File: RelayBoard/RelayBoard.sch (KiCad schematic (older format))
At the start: 56 parts, among them J1 Micro_SD_Card, J10 Conn_01x04_Male, J11 Conn_01x04_Male, J13 Conn_01x04_Male, J2 Screw_Terminal_01x02, J3 Conn_01x04_Male, J4 Conn_01x04_Male, J5 Conn_01x04_Male, J7 SI-52008-F, J8 SI-52008-F, J9 Conn_01x04_Male, U1 STM32F745VEHx, U2 KSZ8863RLL, U3 TJA1051T-3, U4 LF33_TO252, X1 ECS-2520MV-xxx-xx

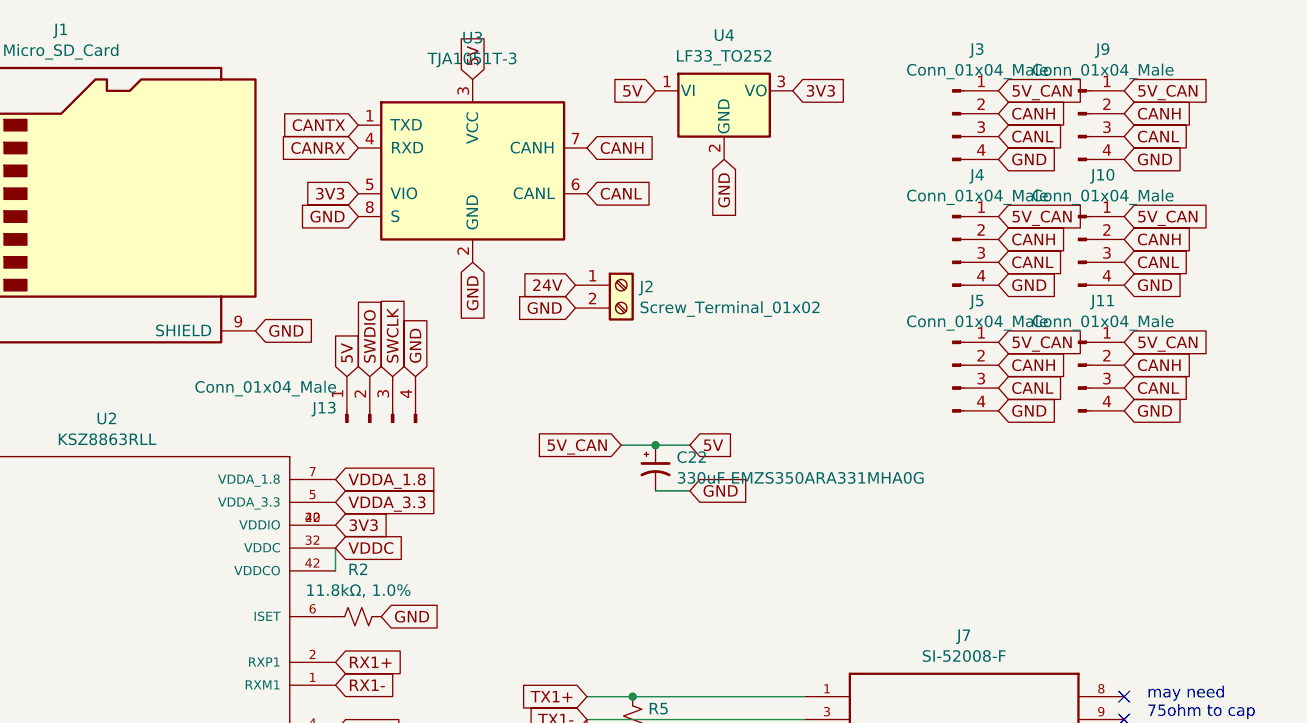
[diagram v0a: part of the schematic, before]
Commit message: unnecessary but satisfying miniaturization
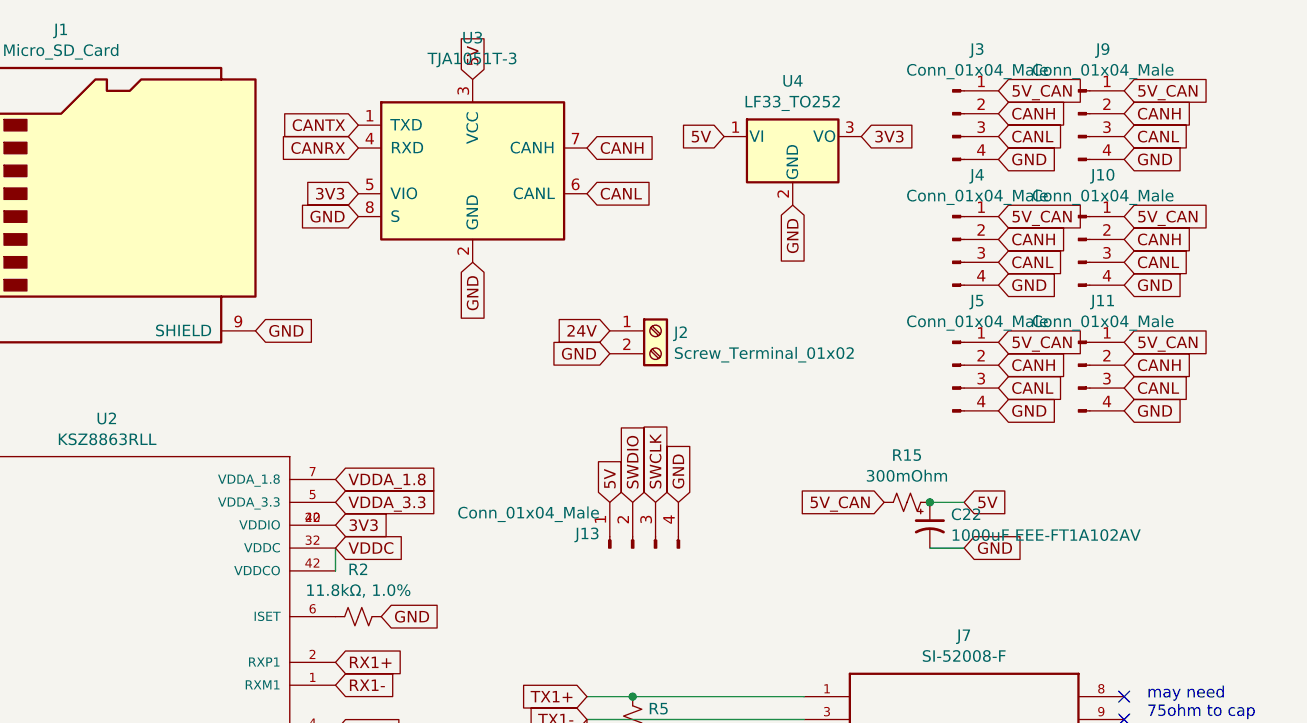
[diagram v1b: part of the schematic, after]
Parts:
- added R15: 300mOhm, symbol Device:R_Small_US
- C22: value 330uF EMZS350ARA331MHA0G -> 1000uF EEE-FT1A102AV; footprint Capacitor_SMD:CP_Elec_10x10 -> Capacitor_SMD:CP_Elec_8x10.5
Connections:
- net +5V: now also R15.1; no longer J10.1 (Pin_1), J11.1 (Pin_1), J3.1 (Pin_1), J4.1 (Pin_1), J5.1 (Pin_1), J9.1 (Pin_1)
- new net 5V_CAN: J10.1 (Pin_1), J11.1 (Pin_1), J3.1 (Pin_1), J4.1 (Pin_1), J5.1 (Pin_1), J9.1 (Pin_1), R15.2
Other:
- moved on the sheet: C22, J13, J2, U4
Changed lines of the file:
@@
 Comment4 ""
 $EndDescr
-$Comp
-L Connector:Screw_Terminal_01x02 J2
-U 1 1 5E6836EC
-P 7600 1650
-F 0 "J2" H 7680 1642 50  0000 L CNN
-F 1 "Screw_Terminal_01x02" H 7680 1551 50  0000 L CNN
-F 2 "TerminalBlock_Phoenix:TerminalBlock_Phoenix_MKDS-1,5-2_1x02_P5.00mm_Horizontal" H 7600 1650 50  0001 C CNN
-F 3 "~" H 7600 1650 50  0001 C CNN
-	1    7600 1650
-	1    0    0    -1
-$EndComp
 Text GLabel 7450 1050 2    50   Input ~ 0
 CANH
@@
 Text GLabel 6450 1050 0    50   Input ~ 0
 CANRX
-$Comp
-L Interface_CAN_LIN:TJA1051T-3 U3
-U 1 1 5E6B6C50
-P 6950 1150
-F 0 "U3" H 6950 1731 50  0000 C CNN
-F 1 "TJA1051T-3" H 6950 1640 50  0000 C CNN
-F 2 "Package_SO:SOIC-8_3.9x4.9mm_P1.27mm" H 6950 650 50  0001 C CIN
-F 3 "http://www.nxp.com/documents/data_sheet/TJA1051.pdf" H 6950 1150 50  0001 C CNN
-	1    6950 1150
-	1    0    0    -1
-$EndComp
 Text GLabel 6950 1550 3    50   Input ~ 0
 GND
@@
 Text GLabel 6450 1250 0    50   Input ~ 0
 3V3
-Text GLabel 7400 1650 0    50   Input ~ 0
-24V
-Text GLabel 7400 1750 0    50   Input ~ 0
-GND
 $Comp
 L SI-52008-F:SI-52008-F J7
@@
 L Regulator_Linear:LF33_TO252 U4
 U 1 1 5E6D356C
-P 8050 800
-F 0 "U4" H 8050 1042 50  0000 C CNN
-F 1 "LF33_TO252" H 8050 951 50  0000 C CNN
-F 2 "Package_TO_SOT_SMD:TO-252-2" H 8050 1025 50  0001 C CIN
-F 3 "http://www.st.com/content/ccc/resource/technical/document/datasheet/c4/0e/7e/2a/be/bc/4c/bd/CD00000546.pdf/files/CD00000546.pdf/jcr:content/translations/en.CD00000546.pdf" H 8050 750 50  0001 C CNN
-	1    8050 800
-	1    0    0    -1
-$EndComp
-Text GLabel 7750 800  0    50   Input ~ 0
+P 8350 1000
+F 0 "U4" H 8350 1242 50  0000 C CNN
+F 1 "LF33_TO252" H 8350 1151 50  0000 C CNN
+F 2 "Package_TO_SOT_SMD:TO-252-2" H 8350 1225 50  0001 C CIN
+F 3 "http://www.st.com/content/ccc/resource/technical/document/datasheet/c4/0e/7e/2a/be/bc/4c/bd/CD00000546.pdf/files/CD00000546.pdf/jcr:content/translations/en.CD00000546.pdf" H 8350 950 50  0001 C CNN
+	1    8350 1000
+	1    0    0    -1
+$EndComp
+Text GLabel 8050 1000 0    50   Input ~ 0
 5V
-Text GLabel 8350 800  2    50   Input ~ 0
-3V3
-Text GLabel 8050 1100 3    50   Input ~ 0
+Text GLabel 8650 1000 2    50   Input ~ 0
+3V3
+Text GLabel 8350 1300 3    50   Input ~ 0
 GND
 Text GLabel 6000 1850 2    50   Input ~ 0
@@
 L Connector:Conn_01x04_Male J13
 U 1 1 5E67695C
-P 6500 2250
-F 0 "J13" V 6562 2394 50  0000 L CNN
-F 1 "Conn_01x04_Male" V 6653 2394 50  0000 L CNN
-F 2 "Connector_PinHeader_2.54mm:PinHeader_1x04_P2.54mm_Vertical" H 6500 2250 50  0001 C CNN
-F 3 "~" H 6500 2250 50  0001 C CNN
-	1    6500 2250
+P 7650 2800
+F 0 "J13" V 7712 2944 50  0000 L CNN
+F 1 "Conn_01x04_Male" V 7803 2944 50  0000 L CNN
+F 2 "Connector_PinHeader_2.54mm:PinHeader_1x04_P2.54mm_Vertical" H 7650 2800 50  0001 C CNN
+F 3 "~" H 7650 2800 50  0001 C CNN
+	1    7650 2800
 	0    -1   -1   0
 $EndComp
-Text GLabel 6400 2050 1    50   Input ~ 0
+Text GLabel 7550 2600 1    50   Input ~ 0
 5V
-Text GLabel 6500 2050 1    50   Input ~ 0
+Text GLabel 7650 2600 1    50   Input ~ 0
 SWDIO
-Text GLabel 6600 2050 1    50   Input ~ 0
+Text GLabel 7750 2600 1    50   Input ~ 0
 SWCLK
-Text GLabel 6700 2050 1    50   Input ~ 0
+Text GLabel 7850 2600 1    50   Input ~ 0
 GND
 Text GLabel 3150 1250 2    50   Input ~ 0
@@
 	3950 5100 4350 5100
 NoConn ~ 4350 5500
+Text GLabel 8750 2600 0    50   Input ~ 0
+5V_CAN
+Connection ~ 8950 2600
+$Comp
+L Device:R_Small_US R15
+U 1 1 5E68BBF1
+P 8850 2600
+F 0 "R15" V 8645 2600 50  0000 C CNN
+F 1 "300mOhm" V 8736 2600 50  0000 C CNN
+F 2 "" H 8850 2600 50  0001 C CNN
+F 3 "~" H 8850 2600 50  0001 C CNN
+	1    8850 2600
+	0    1    1    0
+$EndComp
+Wire Wire Line
+	8950 2800 9100 2800
+Wire Wire Line
+	8950 2600 9100 2600
+Text GLabel 9100 2600 2    50   Input ~ 0
+5V
+Text GLabel 9100 2800 2    50   Input ~ 0
+GND
 $Comp
 L Device:CP1_Small C22
 U 1 1 5E86EE8D
-P 7750 2450
-F 0 "C22" H 7842 2496 50  0000 L CNN
-F 1 "330uF EMZS350ARA331MHA0G" H 7842 2405 50  0000 L CNN
-F 2 "Capacitor_SMD:CP_Elec_10x10" H 7750 2450 50  0001 C CNN
-F 3 "~" H 7750 2450 50  0001 C CNN
-	1    7750 2450
-	1    0    0    -1
-$EndComp
-Text GLabel 7600 2350 0    50   Input ~ 0
-5V_CAN
-Text GLabel 7900 2550 2    50   Input ~ 0
-GND
-Text GLabel 7900 2350 2    50   Input ~ 0
-5V
-Wire Wire Line
-	7600 2350 7750 2350
-Connection ~ 7750 2350
-Wire Wire Line
-	7750 2350 7900 2350
-Wire Wire Line
-	7750 2550 7900 2550
+P 8950 2700
+F 0 "C22" H 9042 2746 50  0000 L CNN
+F 1 "1000uF EEE-FT1A102AV" H 9042 2655 50  0000 L CNN
+F 2 "Capacitor_SMD:CP_Elec_8x10.5" H 8950 2700 50  0001 C CNN
+F 3 "~" H 8950 2700 50  0001 C CNN
+	1    8950 2700
+	1    0    0    -1
+$EndComp
+$Comp
+L Connector:Screw_Terminal_01x02 J2
+U 1 1 5E6836EC
+P 7750 1850
+F 0 "J2" H 7830 1842 50  0000 L CNN
+F 1 "Screw_Terminal_01x02" H 7830 1751 50  0000 L CNN
+F 2 "TerminalBlock_Phoenix:TerminalBlock_Phoenix_MKDS-1,5-2_1x02_P5.00mm_Horizontal" H 7750 1850 50  0001 C CNN
+F 3 "~" H 7750 1850 50  0001 C CNN
+	1    7750 1850
+	1    0    0    -1
+$EndComp
+$Comp
+L Interface_CAN_LIN:TJA1051T-3 U3
+U 1 1 5E6B6C50
+P 6950 1150
+F 0 "U3" H 6950 1731 50  0000 C CNN
+F 1 "TJA1051T-3" H 6950 1640 50  0000 C CNN
+F 2 "Package_SO:SOIC-8_3.9x4.9mm_P1.27mm" H 6950 650 50  0001 C CIN
+F 3 "http://www.nxp.com/documents/data_sheet/TJA1051.pdf" H 6950 1150 50  0001 C CNN
+	1    6950 1150
+	1    0    0    -1
+$EndComp
+Text GLabel 7550 1850 0    50   Input ~ 0
+24V
+Text GLabel 7550 1950 0    50   Input ~ 0
+GND
 $EndSCHEMATC

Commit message: ... and now it's even smaller.
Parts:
- removed J10, J11, J4, J5, J9: Conn_01x04_Male, Connector_JST:JST_XH_B4B-XH-AM_1x04_P2.50mm_Vertical, symbol Connector:Conn_01x04_Male
- added J10, J11, J12, J4: 505004-0812, SamacSys_Parts:5050040812, symbol SamacSys_Parts:505004-0812
- R15: footprint (none) -> Resistor_SMD:R_0805_2012Metric_Pad1.15x1.40mm_HandSolder
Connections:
- net +5V: no longer J13.1 (Pin_1)
- net 5V_CAN: now also J13.1 (Pin_1), J4.P1 (POWER_1), J4.P2 (POWER_2)
- net CANH: now also J4.S1 (SIGNAL_1), J4.S4 (SIGNAL_4)
- net CANL: now also J4.S2 (SIGNAL_2), J4.S3 (SIGNAL_3)
- net GND: now also J10.P1 (POWER_1), J10.P2 (POWER_2), J10.P3 (POWER_3), J10.P4 (POWER_4), J11.P1 (POWER_1), J11.P2 (POWER_2), J11.P3 (POWER_3), J11.P4 (POWER_4), J12.P1 (POWER_1), J12.P2 (POWER_2), J12.P3 (POWER_3), J12.P4 (POWER_4), J4.MP1, J4.MP2, J4.MP3, J4.MP4, J4.P3 (POWER_3), J4.P4 (POWER_4)
- no-connect marks 80 -> 104
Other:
- moved on the sheet: C22, J13, J2, J3, R15

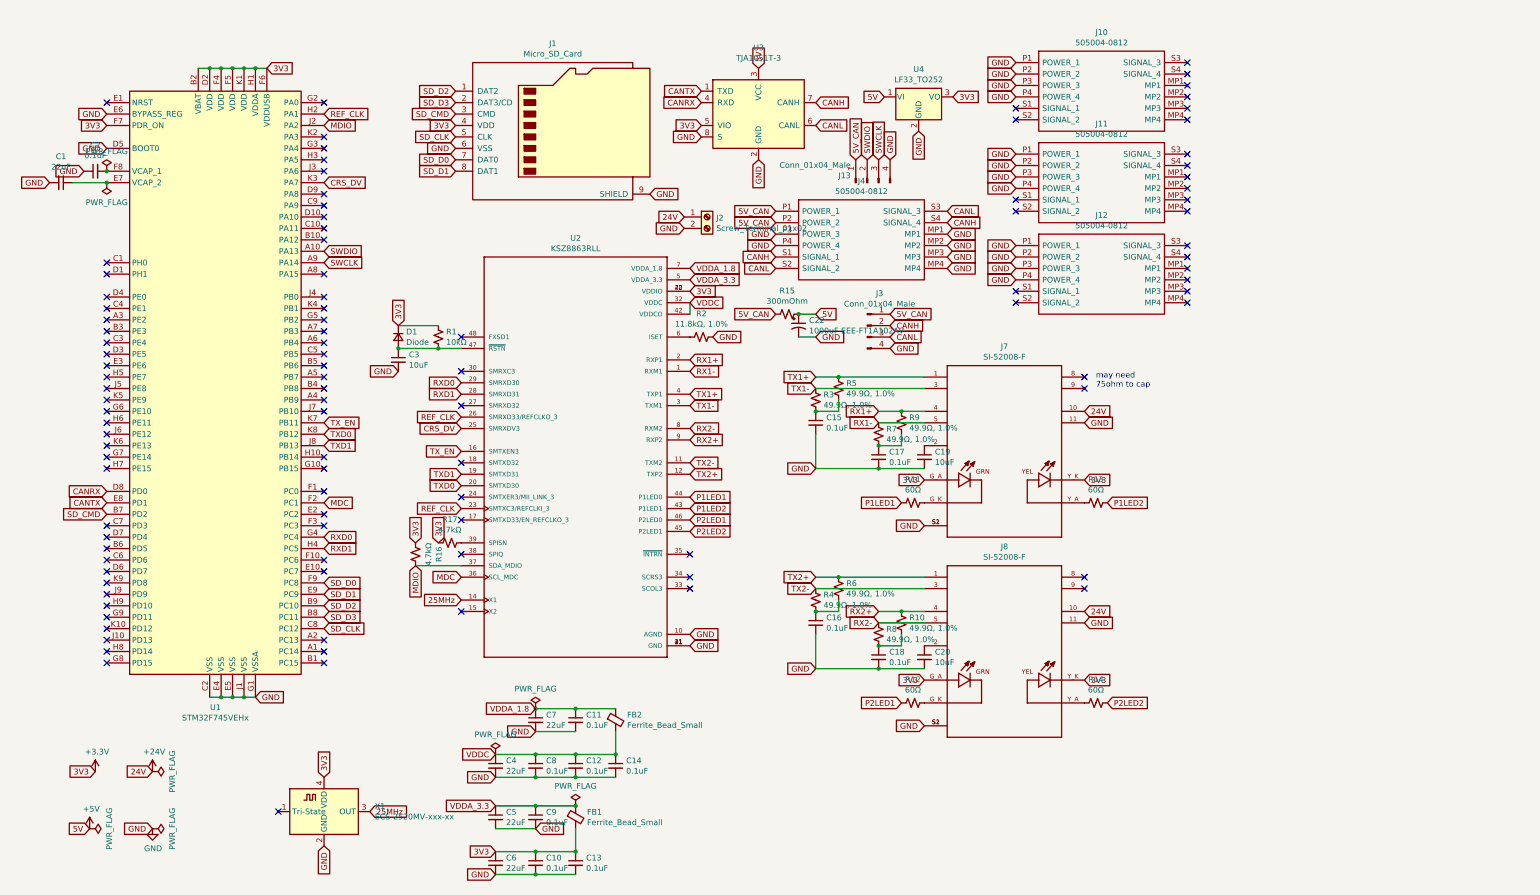
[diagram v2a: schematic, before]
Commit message: better grounding etc
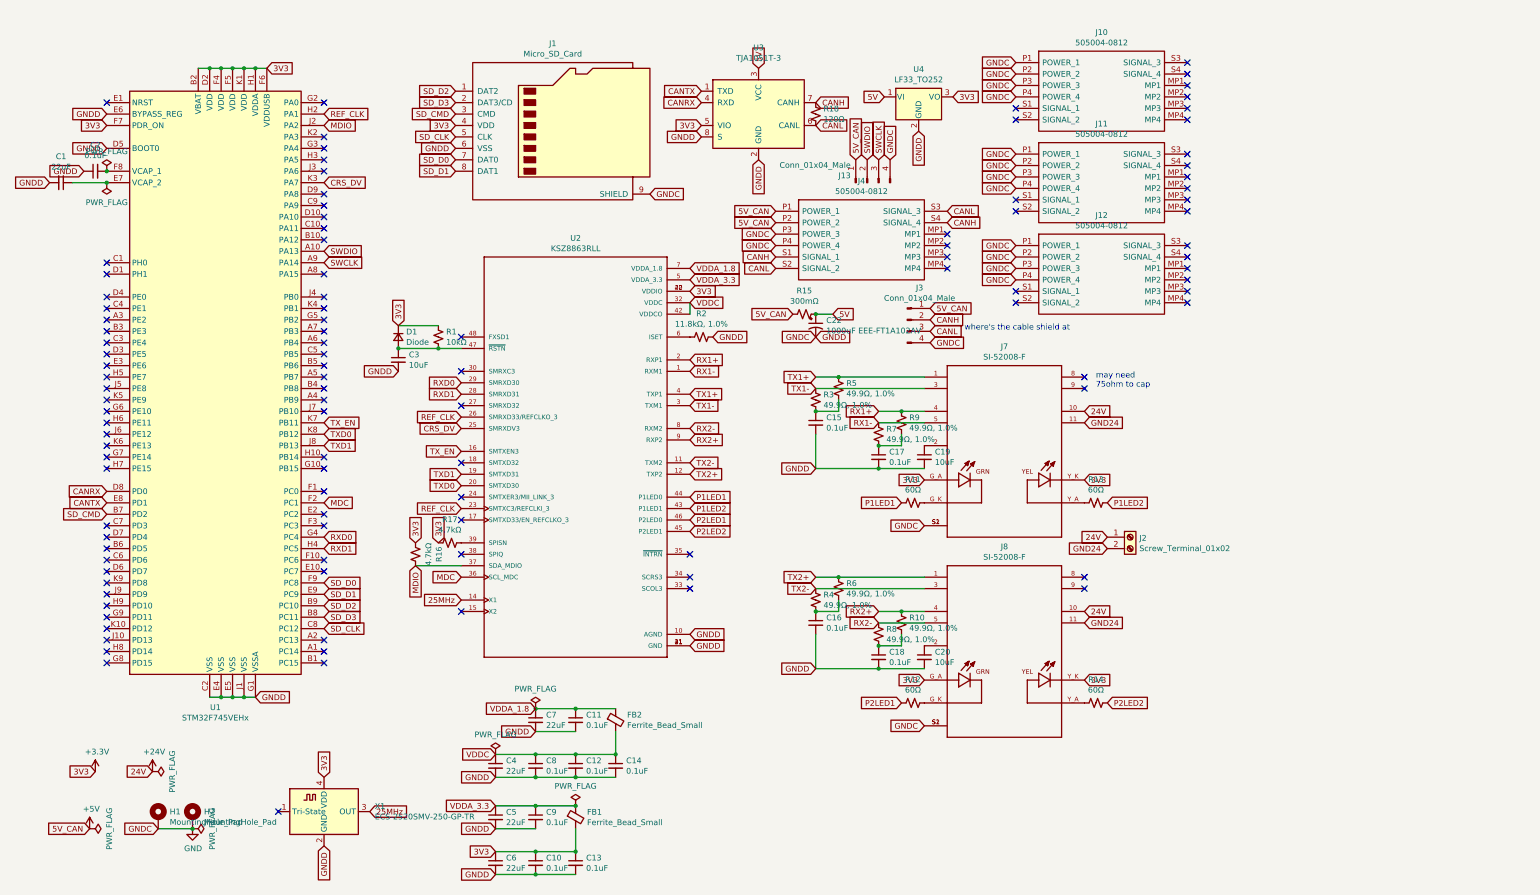
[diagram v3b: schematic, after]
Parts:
- added H1, H2: MountingHole_Pad, MountingHole:MountingHole_3.2mm_M3_Pad_Via, symbol Mechanical:MountingHole_Pad
- added R18: 120Ω, Resistor_SMD:R_0603_1608Metric_Pad1.05x0.95mm_HandSolder, symbol Device:R_Small_US
- R15: value 300mOhm -> 300mΩ
- X1: value ECS-2520MV-xxx-xx -> ECS-2520SMV-250-GP-TR
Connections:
- net 5V_CAN is gone; now on net +5V: J13.1 (Pin_1), J3.1 (Pin_1), J4.P1 (POWER_1), J4.P2 (POWER_2), R15.2
- net +5V: no longer C22.1, R15.1, U3.3 (VCC), U4.1 (VI)
- net CANH: now also R18.1
- net CANL: now also R18.2
- net GND: now also H1.1, H2.1; no longer J2.2 (Pin_2), J4.MP1, J4.MP2, J4.MP3, J4.MP4, J7.11 (VC-_P11), J8.11 (VC-_P11)
- new net 5V: C22.1, R15.1, U3.3 (VCC), U4.1 (VI)
- new net GND24: J2.2 (Pin_2), J7.11 (VC-_P11), J8.11 (VC-_P11)
- no-connect marks 104 -> 108
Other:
- note added: "where's the cable shield at"
- moved on the sheet: C22, J2, J3, R15

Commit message: final edits during sourcing; submitted for printing
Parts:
- J1: footprint Connector_Card:microSD_HC_Wuerth_693072010801 -> SamacSys_Parts:PJS008U30000; symbol Connector:Micro_SD_Card -> SamacSys_Parts:PJS008U-3000-0
- J2: footprint TerminalBlock_Phoenix:TerminalBlock_Phoenix_MKDS-1,5-2_1x02_P5.00mm_Horizontal -> SamacSys_Parts:1725656; symbol Connector:Screw_Terminal_01x02 -> SamacSys_Parts:1725656
- J3: footprint Connector_JST:JST_XH_B4B-XH-AM_1x04_P2.50mm_Vertical -> Connector_JST:JST_XH_B4B-XH-A_1x04_P2.50mm_Vertical
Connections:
- net +24V: now also J2.2; no longer J2.1 (Pin_1)
- net CANH: now also J4.S2 (SIGNAL_2), J4.S3 (SIGNAL_3); no longer J4.S1 (SIGNAL_1), J4.S4 (SIGNAL_4)
- net CANL: now also J4.S1 (SIGNAL_1), J4.S4 (SIGNAL_4); no longer J4.S2 (SIGNAL_2), J4.S3 (SIGNAL_3)
- net GND: now also J1.MH1, J1.MH2; no longer J1.9 (SHIELD)
- net GND24: now also J2.1; no longer J2.2 (Pin_2)
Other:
- moved on the sheet: C15, C16, C17, C18, C19, C20, J7, J8, R10, R11, R12, R13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

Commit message: update relayboard
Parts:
- removed J1: Micro_SD_Card, SamacSys_Parts:PJS008U30000, symbol SamacSys_Parts:PJS008U-3000-0
- removed J2: Screw_Terminal_01x02, SamacSys_Parts:1725656, symbol SamacSys_Parts:1725656
- added J? (x5): Conn_01x04_Male, Connector_JST:JST_XH_B4B-XH-A_1x04_P2.50mm_Vertical, symbol Connector:Conn_01x04_Male
- added J?: Micro_SD_Card_Det_Hirose_DM3AT, symbol Connector:Micro_SD_Card_Det_Hirose_DM3AT
- added Q?: XT60_YELLOW, AMASS_XT60PB-M, symbol XT_60:XT60_YELLOW
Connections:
- net +24V: now also Q?.1
- net +3V3: now also J?.4 (VDD)
- net +5V: now also J?.1 (Pin_1), J?.1 (Pin_1), J?.1 (Pin_1), J?.1 (Pin_1), J?.1 (Pin_1)
- net CANH: now also J?.2 (Pin_2), J?.2 (Pin_2), J?.2 (Pin_2), J?.2 (Pin_2), J?.2 (Pin_2)
- net CANL: now also J?.3 (Pin_3), J?.3 (Pin_3), J?.3 (Pin_3), J?.3 (Pin_3), J?.3 (Pin_3)
- net GND: now also J?.11 (SHIELD), J?.4 (Pin_4), J?.4 (Pin_4), J?.4 (Pin_4), J?.4 (Pin_4), J?.4 (Pin_4), J?.6 (VSS)
- net GND24: now also Q?.2
- net SD_CLK: now also J?.5 (CLK)
- net SD_CMD: now also J?.3 (CMD)
- net SD_D0: now also J?.7 (DAT0)
- net SD_D1: now also J?.8 (DAT1)
- net SD_D2: now also J?.1 (DAT2)
- net SD_D3: now also J?.2 (DAT3/CD)
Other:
- note added: "where does the cable shielding connect"
- note removed: "where's the cable shield at"
- moved on the sheet: J13, J3, R18, U3, U4
